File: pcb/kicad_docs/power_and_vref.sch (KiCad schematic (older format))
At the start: 24 parts, among them J7 power_input, U1 SSM2164, U2 TL072, U3 TL072, U4 TL072, U5 TL072, U6 MAX6035xxUR50

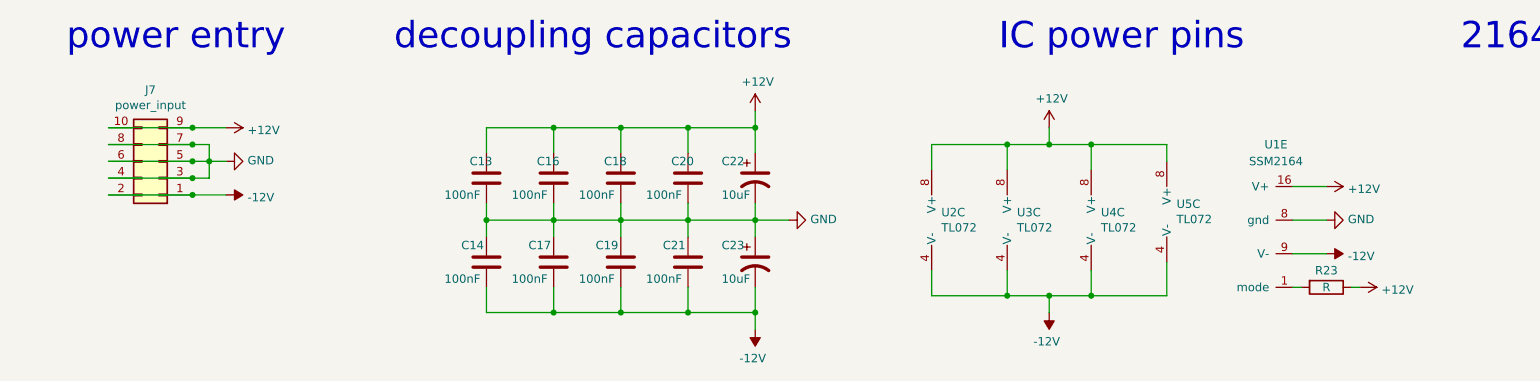
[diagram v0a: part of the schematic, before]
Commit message: add panel, generate interactive BOM
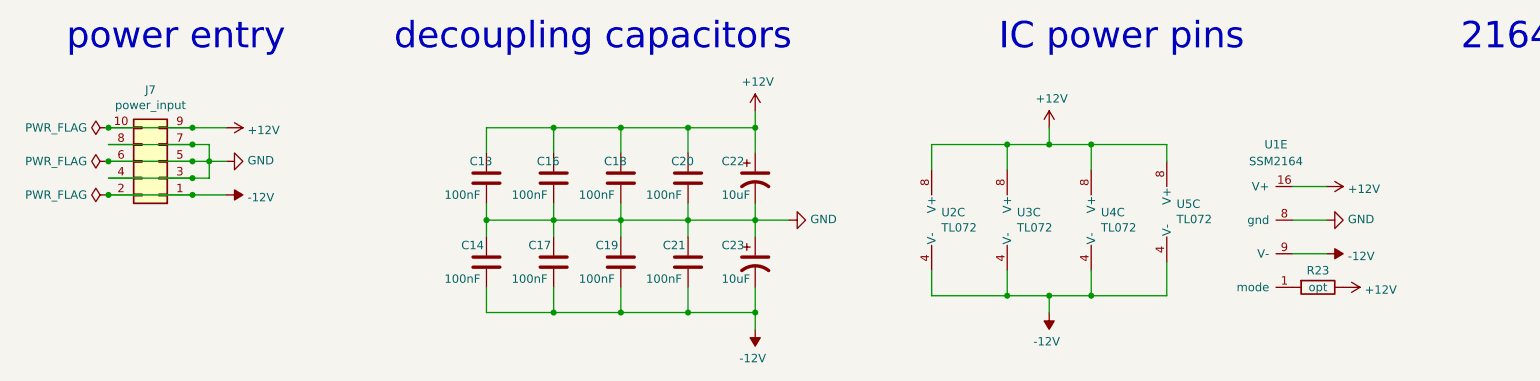
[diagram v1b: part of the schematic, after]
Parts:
- R23: value R -> opt
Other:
- moved on the sheet: R23
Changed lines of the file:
@@
 Sheet 4 4
 Title "Dual VCA power and vref components"
-Date "2020-02-08"
+Date "2020-07-13"
 Rev "1"
 Comp ""
@@
 L Device:R R?
 U 1 1 5E6E7316
-P 8300 5900
+P 8250 5900
 AR Path="/5E6E7316" Ref="R?"  Part="1"
 AR Path="/5E6A7940/5E6E7316" Ref="R23"  Part="1"
-F 0 "R23" V 8200 5900 50  0000 C CNN
-F 1 "R" V 8300 5900 50  0000 C CNN
-F 2 "Resistor_SMD:R_0805_2012Metric_Pad1.15x1.40mm_HandSolder" V 8230 5900 50  0001 C CNN
-F 3 "~" H 8300 5900 50  0001 C CNN
-	1    8300 5900
-	0    1    1    0
-$EndComp
-Wire Wire Line
-	8150 5900 8100 5900
+F 0 "R23" V 8150 5900 50  0000 C CNN
+F 1 "opt" V 8250 5900 50  0000 C CNN
+F 2 "Resistor_SMD:R_0805_2012Metric_Pad1.15x1.40mm_HandSolder" V 8180 5900 50  0001 C CNN
+F 3 "~" H 8250 5900 50  0001 C CNN
+	1    8250 5900
+	0    1    1    0
+$EndComp
 $Comp
 L power:+12V #PWR?
 U 1 1 5E6E731D
-P 8500 5900
+P 8400 5900
 AR Path="/5E6E731D" Ref="#PWR?"  Part="1"
 AR Path="/5E6A7940/5E6E731D" Ref="#PWR035"  Part="1"
-F 0 "#PWR035" H 8500 5750 50  0001 C CNN
-F 1 "+12V" V 8515 6028 50  0000 L CNN
-F 2 "" H 8500 5900 50  0001 C CNN
-F 3 "" H 8500 5900 50  0001 C CNN
-	1    8500 5900
-	0    1    1    0
-$EndComp
-Wire Wire Line
-	8500 5900 8450 5900
+F 0 "#PWR035" H 8400 5750 50  0001 C CNN
+F 1 "+12V" V 8415 6028 50  0000 L CNN
+F 2 "" H 8400 5900 50  0001 C CNN
+F 3 "" H 8400 5900 50  0001 C CNN
+	1    8400 5900
+	0    1    1    0
+$EndComp
 $Comp
 L power:GND #PWR?
@@
 Text Notes 9100 4500 0    157  ~ 0
 2164 protection
+$Comp
+L power:PWR_FLAG #FLG0101
+U 1 1 5F0D7AE2
+P 1050 4950
+F 0 "#FLG0101" H 1050 5025 50  0001 C CNN
+F 1 "PWR_FLAG" V 1050 5077 50  0000 L CNN
+F 2 "" H 1050 4950 50  0001 C CNN
+F 3 "~" H 1050 4950 50  0001 C CNN
+	1    1050 4950
+	0    -1   -1   0
+$EndComp
+Connection ~ 1050 4950
+$Comp
+L power:PWR_FLAG #FLG0102
+U 1 1 5F0D97C8
+P 1050 5150
+F 0 "#FLG0102" H 1050 5225 50  0001 C CNN
+F 1 "PWR_FLAG" V 1050 5277 50  0000 L CNN
+F 2 "" H 1050 5150 50  0001 C CNN
+F 3 "~" H 1050 5150 50  0001 C CNN
+	1    1050 5150
+	0    -1   -1   0
+$EndComp
+Connection ~ 1050 5150
+$Comp
+L power:PWR_FLAG #FLG0103
+U 1 1 5F0D9927
+P 1050 5350
+F 0 "#FLG0103" H 1050 5425 50  0001 C CNN
+F 1 "PWR_FLAG" V 1050 5477 50  0000 L CNN
+F 2 "" H 1050 5350 50  0001 C CNN
+F 3 "~" H 1050 5350 50  0001 C CNN
+	1    1050 5350
+	0    -1   -1   0
+$EndComp
+Connection ~ 1050 5350
 $EndSCHEMATC
